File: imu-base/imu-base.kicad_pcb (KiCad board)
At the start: 2 copper layers, 44 x 44 mm, 20 parts, among them J1 1374028, J2 DE9_Plug_MountingHoles, U1 AP2204K-ADJ

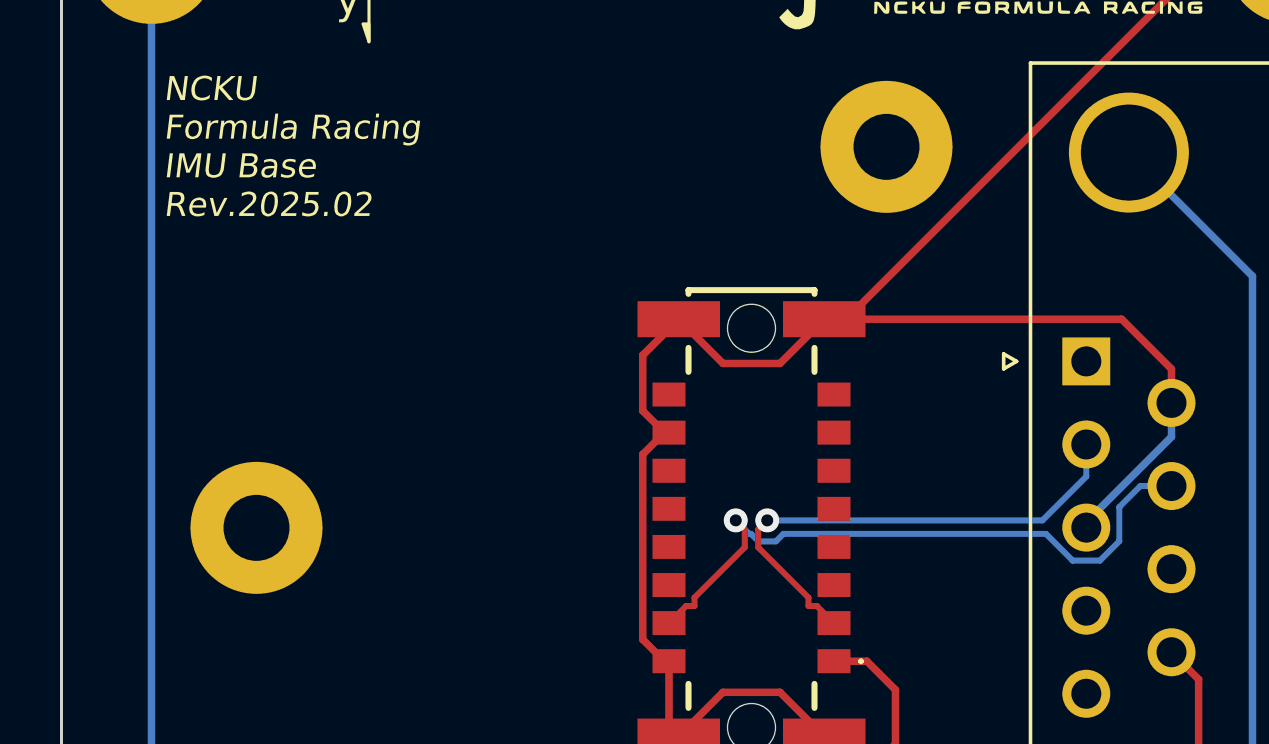
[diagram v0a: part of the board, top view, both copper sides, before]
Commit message: fix: CAN pin error
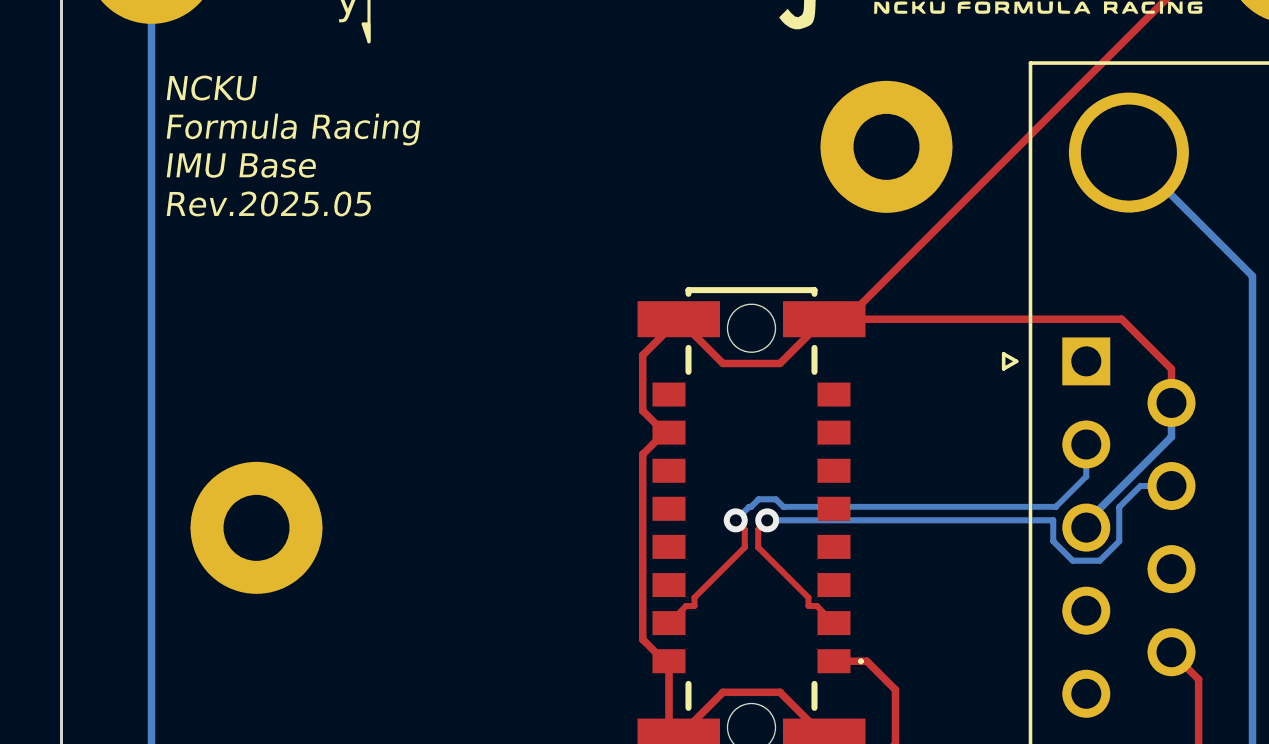
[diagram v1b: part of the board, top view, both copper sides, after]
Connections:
- J2 pad 2: CAN_P -> CAN_N
- J2 pad 7: CAN_N -> CAN_P
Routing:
- net CAN_P: track 17.1 -> 20.9 mm
- net CAN_N: track 21.7 -> 18.3 mm
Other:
- board text added: "NCKU Formula Racing IMU Base Rev.2025.05"
- board text removed: "NCKU Formula Racing IMU Base Rev.2025.02"
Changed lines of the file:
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@@
       (net 16 "unconnected-(J2-Pad1)") (pinfunction "1") (pintype "passive+no_connect"))
     (pad "2" thru_hole circle (at -2.77 0 90) (size 1.6 1.6) (drill 1) (layers "*.Cu" "*.Mask")
-      (net 18 "CAN_P") (pinfunction "2") (pintype "passive"))
+      (net 21 "CAN_N") (pinfunction "2") (pintype "passive"))
     (pad "3" thru_hole circle (at -5.54 0 90) (size 1.6 1.6) (drill 1) (layers "*.Cu" "*.Mask")
       (net 1 "GND") (pinfunction "3") (pintype "passive"))
@@
       (net 1 "GND") (pinfunction "6") (pintype "passive"))
     (pad "7" thru_hole circle (at -4.155 2.84 90) (size 1.6 1.6) (drill 1) (layers "*.Cu" "*.Mask")
-      (net 21 "CAN_N") (pinfunction "7") (pintype "passive"))
+      (net 18 "CAN_P") (pinfunction "7") (pintype "passive"))
     (pad "8" thru_hole circle (at -6.925 2.84 90) (size 1.6 1.6) (drill 1) (layers "*.Cu" "*.Mask")
       (net 23 "unconnected-(J2-Pad8)") (pinfunction "8") (pintype "passive+no_connect"))
@@
     (effects (font (size 1 1) (thickness 0.1)))
   )
-  (gr_text "NCKU\nFormula Racing\nIMU Base\nRev.2025.02" (at 76.4 47.7) (layer "F.SilkS")
+  (gr_text "NCKU\nFormula Racing\nIMU Base\nRev.2025.05" (at 76.4 47.7) (layer "F.SilkS")
     (effects (font (size 0.8 0.8) (thickness 0.12) italic) (justify left bottom))
   )
@@
   (segment (start 96.225001 58.049999) (end 96.525 57.75) (width 0.2) (layer "F.Cu") (net 18))
   (via (at 96.525 57.75) (size 0.8) (drill 0.4) (layers "F.Cu" "B.Cu") (net 18))
-  (segment (start 105.696801 57.75) (end 107.16 56.286801) (width 0.2) (layer "B.Cu") (net 18))
-  (segment (start 96.525 57.75) (end 105.696801 57.75) (width 0.2) (layer "B.Cu") (net 18))
-  (segment (start 107.16 56.286801) (end 107.16 55.22) (width 0.2) (layer "B.Cu") (net 18))
+  (segment (start 106.06 57.75) (end 106.06 58.445635) (width 0.2) (layer "B.Cu") (net 18))
+  (segment (start 108.26 57.30741) (end 108.96241 56.605) (width 0.2) (layer "B.Cu") (net 18))
+  (segment (start 96.525 57.75) (end 106.06 57.75) (width 0.2) (layer "B.Cu") (net 18))
+  (segment (start 106.704365 59.09) (end 107.615635 59.09) (width 0.2) (layer "B.Cu") (net 18))
+  (segment (start 106.06 58.445635) (end 106.704365 59.09) (width 0.2) (layer "B.Cu") (net 18))
+  (segment (start 107.615635 59.09) (end 108.26 58.445635) (width 0.2) (layer "B.Cu") (net 18))
+  (segment (start 108.96241 56.605) (end 110 56.605) (width 0.2) (layer "B.Cu") (net 18))
+  (segment (start 108.26 58.445635) (end 108.26 57.30741) (width 0.2) (layer "B.Cu") (net 18))
   (segment (start 94.1 60.325) (end 95.774999 58.650001) (width 0.2) (layer "F.Cu") (net 21))
   (segment (start 95.774999 58.049999) (end 95.475 57.75) (width 0.2) (layer "F.Cu") (net 21))
@@
   (segment (start 93.25 61.175) (end 93.82 60.605) (width 0.2) (layer "F.Cu") (net 21))
   (via (at 95.475 57.75) (size 0.8) (drill 0.4) (layers "F.Cu" "B.Cu") (net 21))
-  (segment (start 95.475 57.75) (end 95.925 58.2) (width 0.2) (layer "B.Cu") (net 21))
-  (segment (start 105.814365 58.2) (end 106.704365 59.09) (width 0.2) (layer "B.Cu") (net 21))
-  (segment (start 95.925 58.2) (end 95.98505 58.2) (width 0.2) (layer "B.Cu") (net 21))
-  (segment (start 96.81495 58.45) (end 97.06495 58.2) (width 0.2) (layer "B.Cu") (net 21))
-  (segment (start 95.98505 58.2) (end 96.23505 58.45) (width 0.2) (layer "B.Cu") (net 21))
-  (segment (start 108.96241 56.605) (end 110 56.605) (width 0.2) (layer "B.Cu") (net 21))
-  (segment (start 108.26 57.30741) (end 108.96241 56.605) (width 0.2) (layer "B.Cu") (net 21))
-  (segment (start 108.26 58.445635) (end 108.26 57.30741) (width 0.2) (layer "B.Cu") (net 21))
-  (segment (start 96.23505 58.45) (end 96.81495 58.45) (width 0.2) (layer "B.Cu") (net 21))
-  (segment (start 107.615635 59.09) (end 108.26 58.445635) (width 0.2) (layer "B.Cu") (net 21))
-  (segment (start 106.704365 59.09) (end 107.615635 59.09) (width 0.2) (layer "B.Cu") (net 21))
-  (segment (start 97.06495 58.2) (end 105.814365 58.2) (width 0.2) (layer "B.Cu") (net 21))
+  (segment (start 106.146801 57.3) (end 107.16 56.286801) (width 0.2) (layer "B.Cu") (net 21))
+  (segment (start 95.98505 57.3) (end 96.23505 57.05) (width 0.2) (layer "B.Cu") (net 21))
+  (segment (start 107.16 56.286801) (end 107.16 55.22) (width 0.2) (layer "B.Cu") (net 21))
+  (segment (start 95.475 57.75) (end 95.925 57.3) (width 0.2) (layer "B.Cu") (net 21))
+  (segment (start 96.23505 57.05) (end 96.81495 57.05) (width 0.2) (layer "B.Cu") (net 21))
+  (segment (start 96.81495 57.05) (end 97.06495 57.3) (width 0.2) (layer "B.Cu") (net 21))
+  (segment (start 97.06495 57.3) (end 106.146801 57.3) (width 0.2) (layer "B.Cu") (net 21))
+  (segment (start 95.925 57.3) (end 95.98505 57.3) (width 0.2) (layer "B.Cu") (net 21))
   (segment (start 102.34794 74.7125) (end 102.34794 76.25) (width 0.25) (layer "F.Cu") (net 22))
   (segment (start 100.33544 74.7125) (end 102.34794 74.7125) (width 0.25) (layer "F.Cu") (net 22))
